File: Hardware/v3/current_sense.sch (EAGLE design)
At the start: 38 parts, among them J1 SCREW-TERMINAL_2_0.100, J2 SCREW-TERMINAL_2_0.100, J3 SCREW-TERMINAL_2_0.100, J4 SCREW-TERMINAL_2_0.100, U1 MAX9923H, U2 LP3985

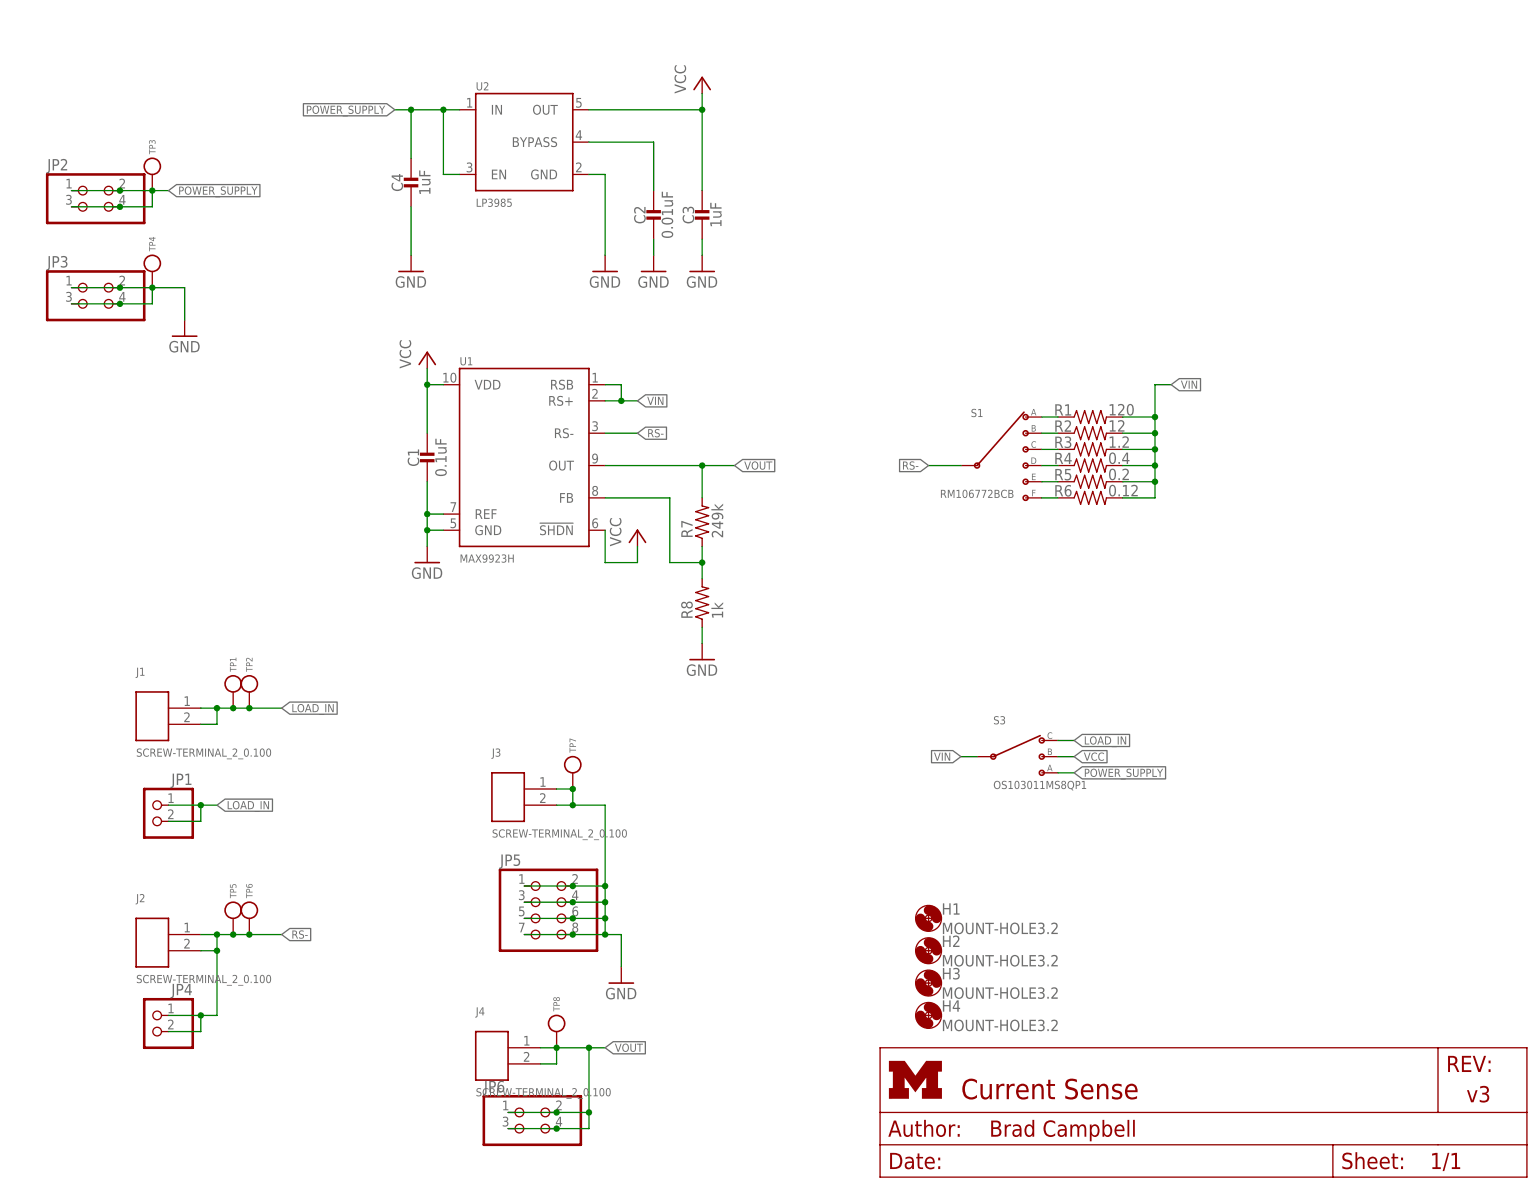
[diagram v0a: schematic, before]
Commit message: better silkscreen
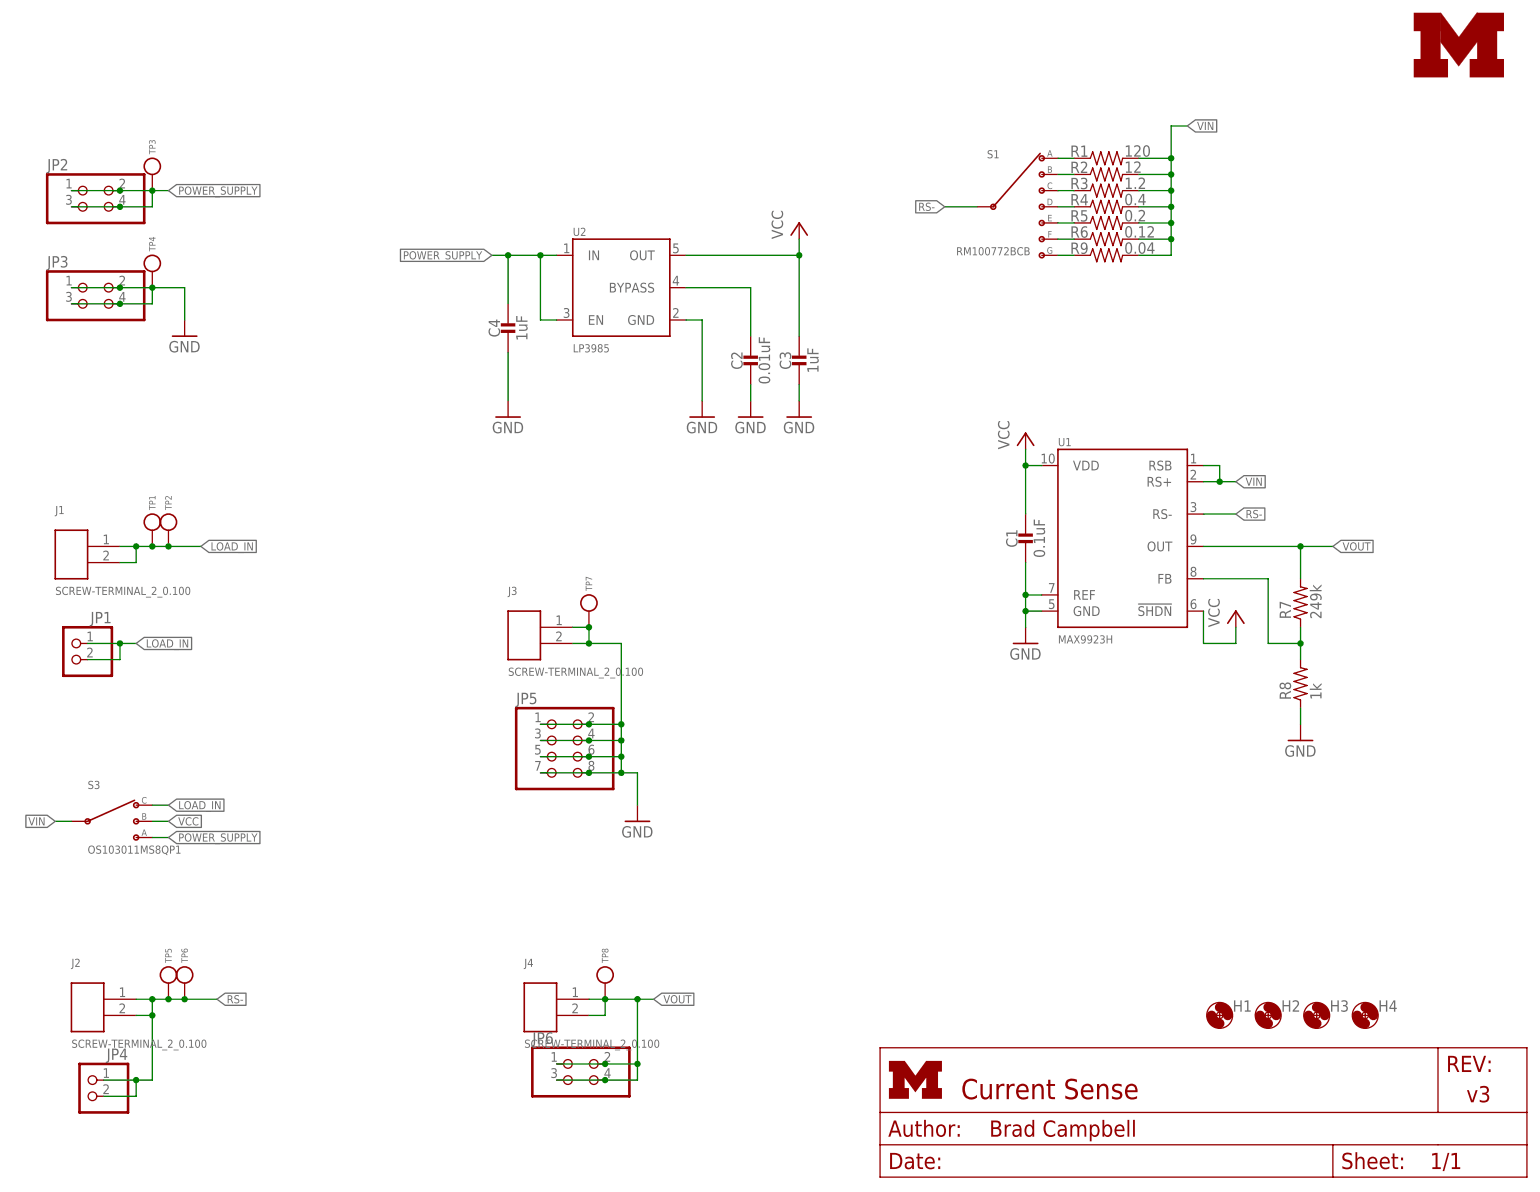
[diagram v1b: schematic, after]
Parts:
- added LOGO2: UMICH_SOLID_MEDIUM, logos:UMICH_SOLID_MEDIUM
- added R9: 0.04, resistor:R-US_R1206
- S1: value RM106772BCB -> RM100772BCB; device switches:RM106772BCB -> switches:RM100772BCB; DIGIKEY (none) -> CKN10705-ND
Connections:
- new net N$9: R9.1, S1.G
- net VIN: now also R9.2
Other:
- note added: "300 mA"
- note added: "Connect to Load"
- note added: "GND"
- note added: "LDO"
- note added: "Load VCC Select"
- note added: "Measurement Output"
- note added: "Power Supply Input"
- note added: "Range Select"
- note added: "Sense Circuitry"
- note added: "Test Input"
- moved on the sheet: C1, C2, C3, C4, H1, H2, H3, H4, J1, J2, J3, J4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

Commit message: renumbered parts and added bom
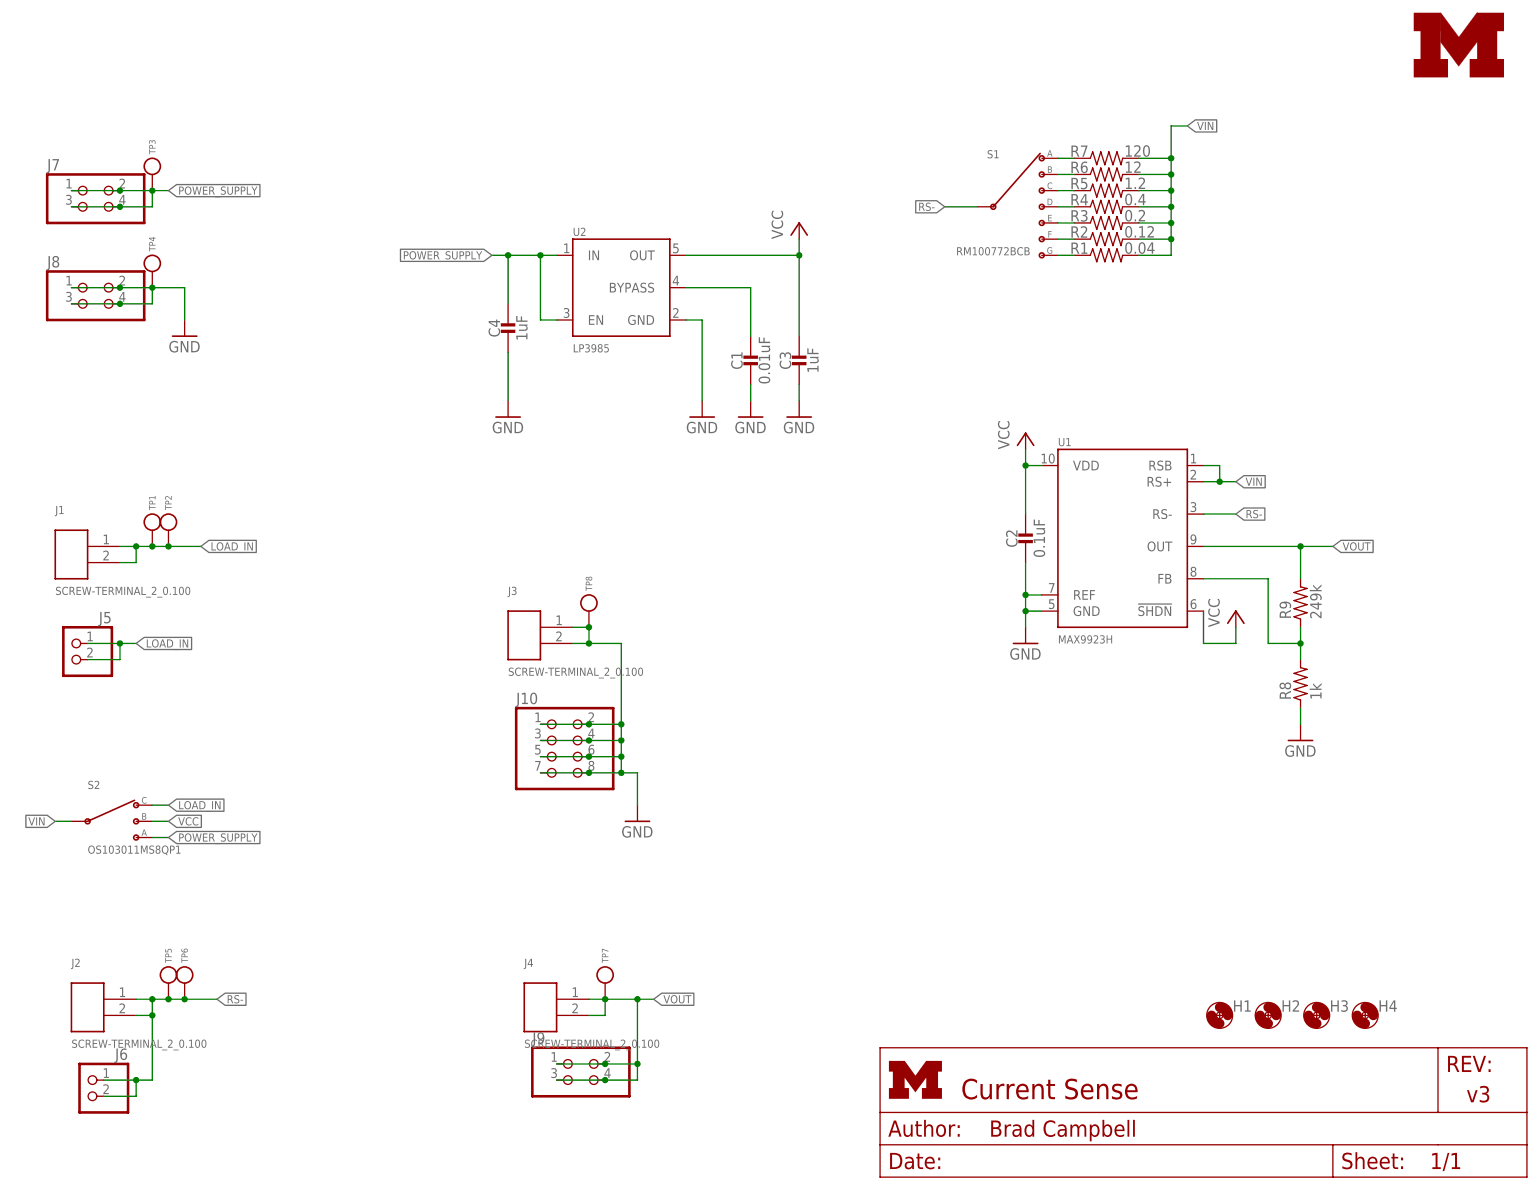
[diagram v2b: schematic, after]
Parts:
- C1: value 0.1uF -> 0.01uF; DIGIKEY 445-1316-1-ND -> 445-5100-1-ND
- C2: value 0.01uF -> 0.1uF; DIGIKEY 445-5100-1-ND -> 445-1316-1-ND
- R1: value 120 -> 0.04; device resistor:R-US_R0805 -> resistor:R-US_R1206; DIGIKEY RG20N120WCT-ND -> 311-.04LWCT-ND
- R2: value 12 -> 0.12; device resistor:R-US_R0805 -> resistor:R-US_R1206; DIGIKEY A103150CT-ND -> RL16R.12FCT-ND
- R3: value 1.2 -> 0.2; device resistor:R-US_R0805 -> resistor:R-US_R1206; DIGIKEY RL12S1.2FCT-ND -> CSR1206FKR200CT-ND
- R5: value 0.2 -> 1.2; device resistor:R-US_R1206 -> resistor:R-US_R0805; DIGIKEY CSR1206FKR200CT-ND -> RL12S1.2FCT-ND
- R6: value 0.12 -> 12; device resistor:R-US_R1206 -> resistor:R-US_R0805; DIGIKEY RL16R.12FCT-ND -> A103150CT-ND
- R7: value 249k -> 120; device passives:RESISTOR0603_RES -> resistor:R-US_R0805; DIGIKEY P249KDBCT-ND -> RG20N120WCT-ND
- R9: value 0.04 -> 249k; device resistor:R-US_R1206 -> passives:RESISTOR0603_RES; DIGIKEY 311-.04LWCT-ND -> P249KDBCT-ND
- TP7: value TEST_POINT_0.112IN -> TEST_POINT_0.040IN; device headers:TEST_POINT_0.112IN -> headers:TEST_POINT_0.040IN
- TP8: value TEST_POINT_0.040IN -> TEST_POINT_0.112IN; device headers:TEST_POINT_0.040IN -> headers:TEST_POINT_0.112IN
- renumbered JP1 to J5, JP2 to J7, JP3 to J8, JP4 to J6, JP5 to J10, JP6 to J9, S3 to S2
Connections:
- net GND: now also TP8.TESTPOINT; no longer TP7.TESTPOINT
- net N$1: now also R7.1; no longer R1.1
- net N$2: now also R6.1; no longer R2.1
- net N$3: now also R5.1; no longer R3.1
- net N$5: now also R3.1; no longer R5.1
- net N$6: now also R2.1; no longer R6.1
- net N$7: now also R9.1; no longer R7.1
- net N$8: now also C1.1; no longer C2.1
- net N$9: now also R1.1; no longer R9.1
- net VCC: now also C2.1; no longer C1.1
- net VIN: now also R7.2; no longer R9.2
- net VOUT: now also R9.2, TP7.TESTPOINT; no longer R7.2, TP8.TESTPOINT
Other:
- moved on the sheet: C1, C2, R1, R2, R3, R5, R6, R7, R9, TP7, TP8

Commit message: updated current sense and zips
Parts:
- U1: DIGIKEY (none) -> MAX9922EUB+TCT-ND
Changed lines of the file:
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@@
 <parts>
 <part name="FRAME1" library="lab11-frames" deviceset="LETTER_L_UMICH" device=""/>
-<part name="U1" library="chips" deviceset="MAX992" device="3H"/>
+<part name="U1" library="chips" deviceset="MAX992" device="3H">
+<attribute name="DIGIKEY" value="MAX9922EUB+TCT-ND"/>
+</part>
 <part name="GND1" library="supply1" deviceset="GND" device=""/>
 <part name="P+1" library="supply1" deviceset="VCC" device=""/>
